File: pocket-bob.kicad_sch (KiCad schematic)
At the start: 127 parts, among them J3 Conn_01x18, J4 Conn_01x18, J5 Conn_01x18, J6 Conn_01x18, J7 USB_A, P1 Conn_02x18_Odd_Even, P2 Conn_02x18_Odd_Even, U1 TPD3S014

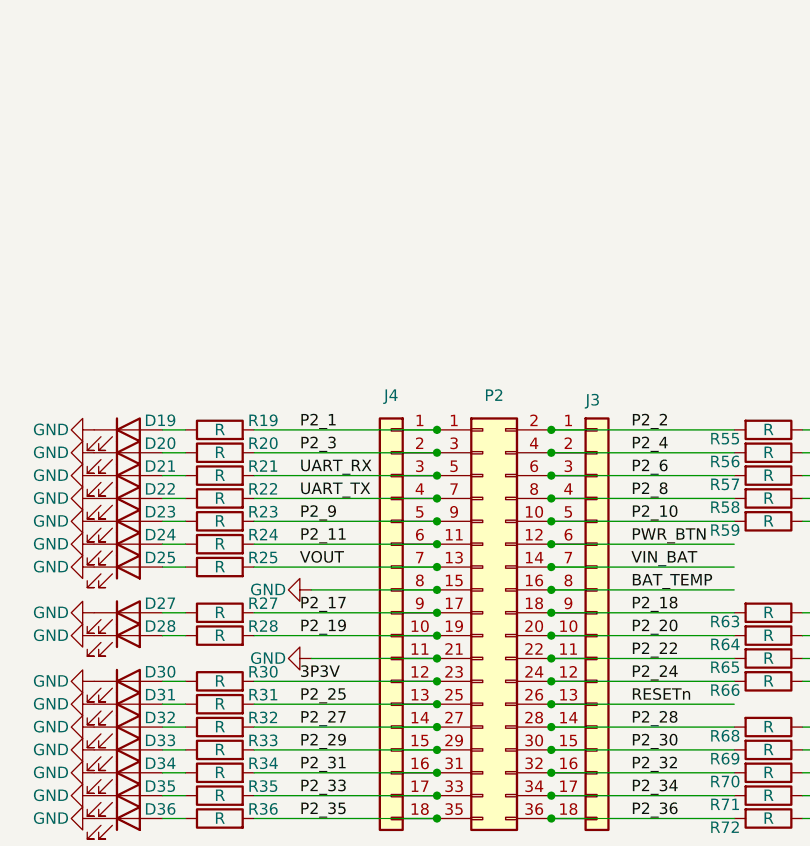
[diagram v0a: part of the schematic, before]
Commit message: Clean up routing and add mounting holes to sch
Signed-off-by: Michael Welling <mwelling79@gmail.com>
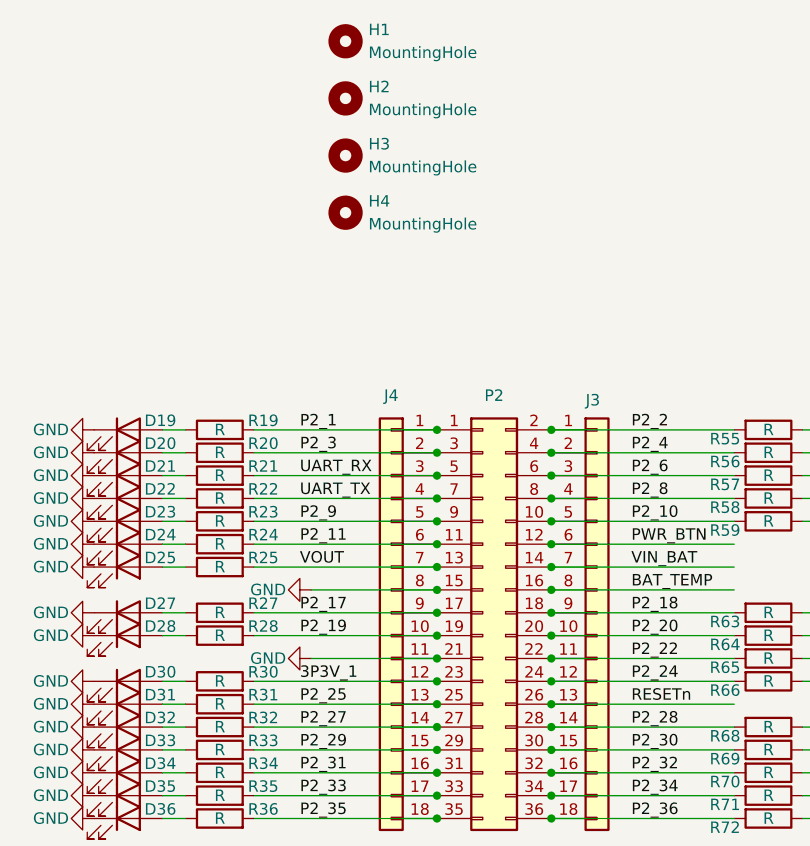
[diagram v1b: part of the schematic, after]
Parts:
- added H1, H2, H3, H4: MountingHole, MountingHole:MountingHole_2.7mm_M2.5, symbol Mechanical:MountingHole
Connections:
- net 3P3V: no longer J4.12 (Pin_12), P2.23 (Pin_23), R30.2
- new net 3P3V_1: J4.12 (Pin_12), P2.23 (Pin_23), R30.2
